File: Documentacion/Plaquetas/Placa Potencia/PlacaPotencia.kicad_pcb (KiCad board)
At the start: 2 copper layers, 145 x 100 mm, 44 parts, among them J1 Conn_01x02_Male, J2 Conn_01x10_Male, Q1 IRF4905, Q2 IRFZ44N, Q3 IRF4905, Q4 IRFZ44N, Q5 BC337, Q6 BC337, U2 MCP1407, U3 MCP1407

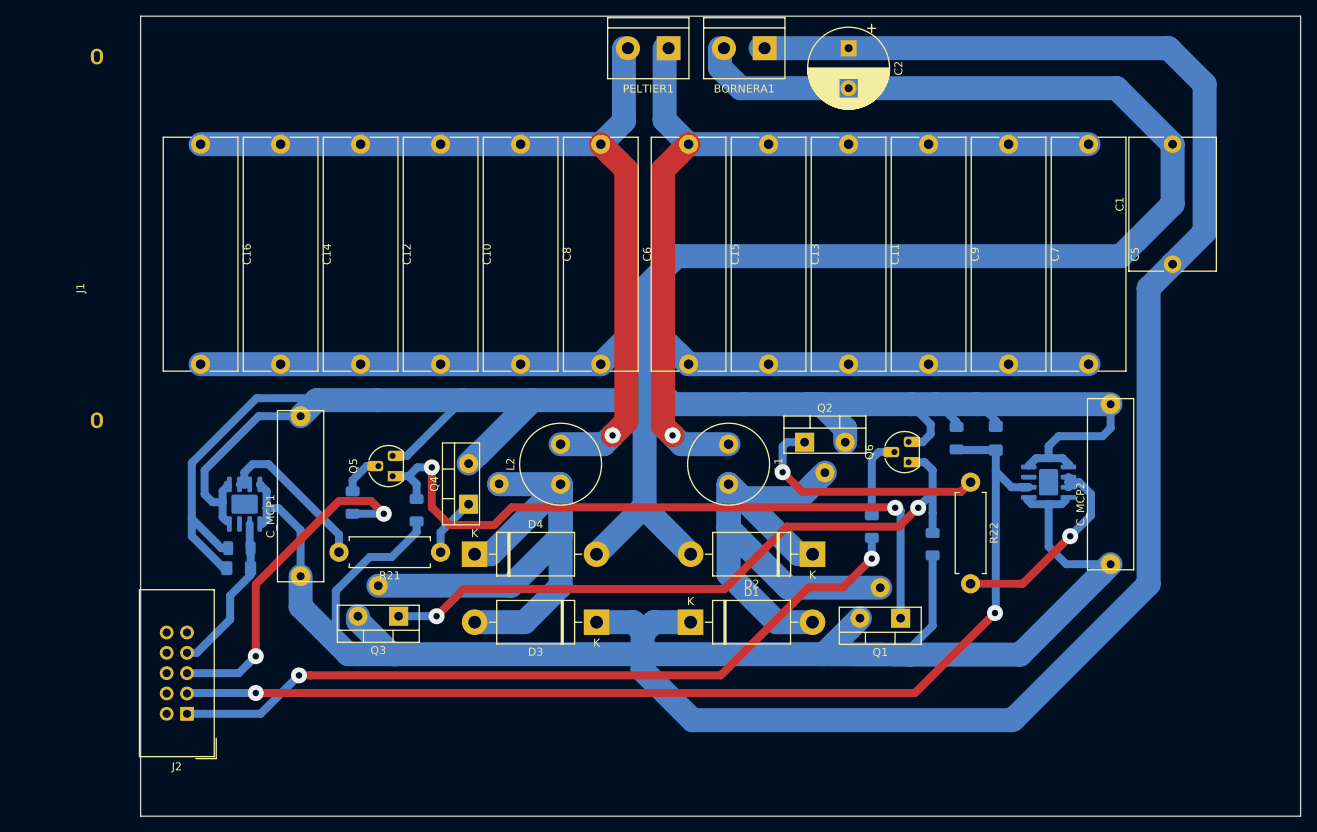
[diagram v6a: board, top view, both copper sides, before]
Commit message: Power PCB changed logic connector, widened traces, added mounting holes
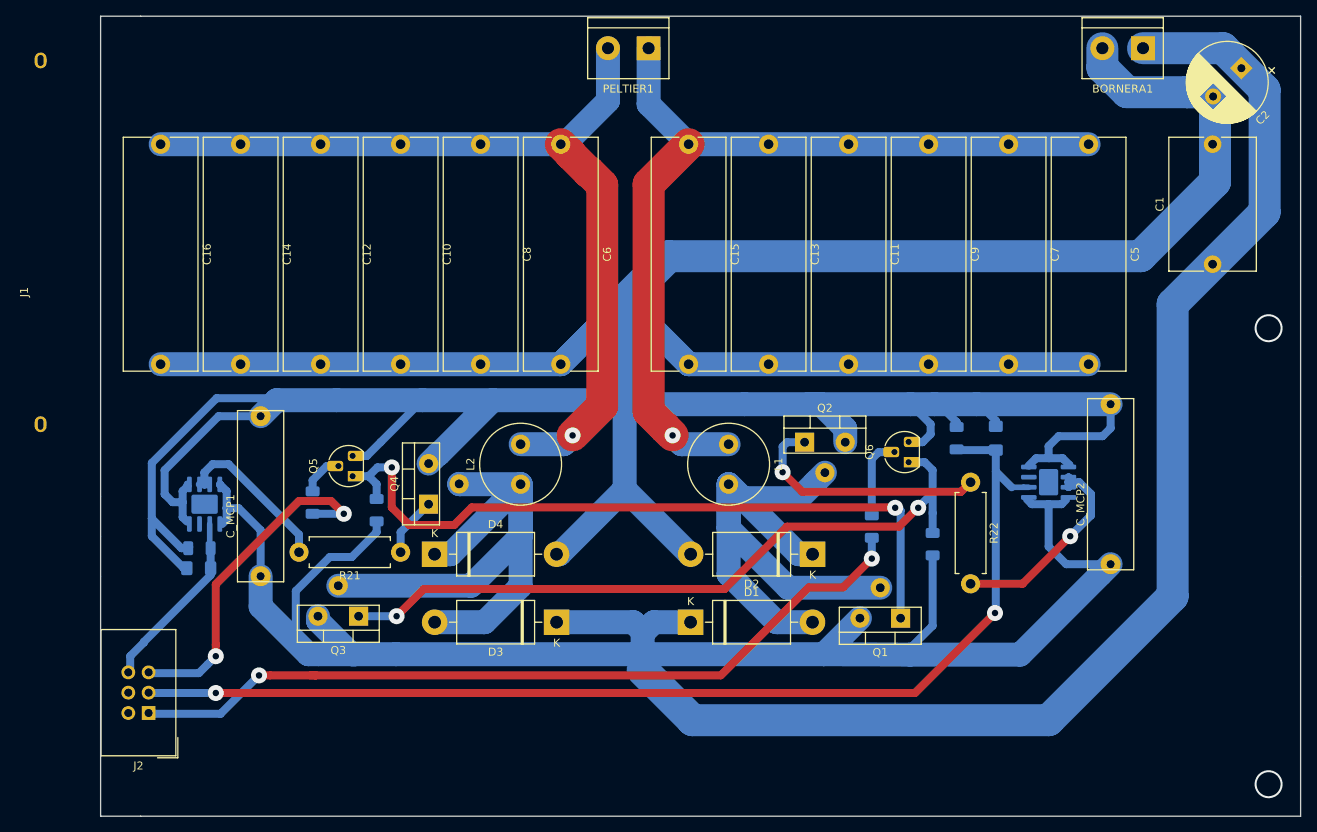
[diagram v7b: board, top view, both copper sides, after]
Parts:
- J2: value Conn_01x10_Male -> Conn_01x06_Male; footprint Connector_IDC:IDC-Header_2x05_P2.54mm_Vertical -> Connector_IDC:IDC-Header_2x03_P2.54mm_Vertical
- moved C2 49.2 mm to (257.6, 41.5), turned to 225 degrees
- moved BORNERA1 47.3 mm to (245.3, 39.0)
- moved J1 7.06 mm to (105.0, 69.5)
- moved C1 5.00 mm to (254.0, 66.0)
- moved C10 5.00 mm to (152.5, 51.0)
- moved C12 5.00 mm to (142.5, 51.0)
- moved C14 5.00 mm to (132.5, 51.0)
- moved C16 5.00 mm to (122.5, 51.0)
- moved C6 5.00 mm to (172.5, 51.0)
- moved C8 5.00 mm to (162.5, 51.0)
- moved C_MCP1 5.00 mm to (135.0, 105.0)
- moved D3 5.00 mm to (172.0, 110.8)
- moved D4 5.00 mm to (156.8, 102.2)
- moved L2 5.00 mm to (167.5, 93.5)
- moved Q3 5.00 mm to (147.2, 110.0)
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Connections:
- J2 pad 6: Net-(J2-Pad6) -> PWM_FRIO
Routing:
- net VCC: track 411.9 -> 387.8 mm
- net GND: track 552.7 -> 560.2 mm
- net PMOS_CALOR: track 96.2 -> 101.9 mm
- net Net-(Q3-Pad1): track 84.4 -> 89.4 mm
- net Net-(Q1-Pad1): track 87.5 -> 92.5 mm
- net PWM_CALOR: track 136.0 -> 140.1 mm
- net PELTIER2: track 108.6 -> 111.8 mm
- net PWM_FRIO: track 20.2 -> 22.9 mm
- net PELTIER1: track 108.9 -> 111.2 mm
- net (no net): vias 0 -> 2
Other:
- board size 145 x 100 mm -> 150 x 100 mm
